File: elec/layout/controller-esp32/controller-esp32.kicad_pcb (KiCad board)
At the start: 2 copper layers, 41 parts, among them U1 10nF ±10% 50V X7R, U10 12.4kΩ ±1% 62.5mW, U11 1nF ±10% 50V X7R, U12 220Ω ±1% 62.5mW, U13 1MΩ ±1% 62.5mW, U15 10pF ±5% 50V C0G, U16 10pF ±5% 50V C0G, U17 100Ω ±1% 62.5mW, U19 10nF ±10% 50V X7R, U2 220Ω ±1% 62.5mW, U20 6.8nF ±10% 50V X7R, U21 33Ω ±1% 62.5mW, U22 49.9Ω ±1% 62.5mW, U23 6.8nF ±10% 50V X7R, U24 33Ω ±1% 62.5mW, U25 49.9Ω ±1% 62.5mW, U26 4.7µF ±10% 10V X5R, U27 22nF ±10% 50V X7R, U28 10Ω ±1% 62.5mW, U29 33Ω ±1% 62.5mW, U3 10µF ±10% 25V X5R, U30 49.9Ω ±1% 62.5mW, U31 33Ω ±1% 62.5mW, U32 49.9Ω ±1% 62.5mW, U34 10µF ±10% 25V X5R, U35 10µF ±10% 25V X5R, U37 10kΩ ±1% 62.5mW, U39 100nF ±10% 16V X7R, U4 100nF ±10% 16V X7R, U41 10kΩ ±1% 62.5mW, U5 100nF ±10% 16V X7R, U6 100nF ±10% 16V X7R, U7 100nF ±10% 16V X7R, U8 100nF ±10% 16V X7R, U9 100nF ±10% 16V X7R

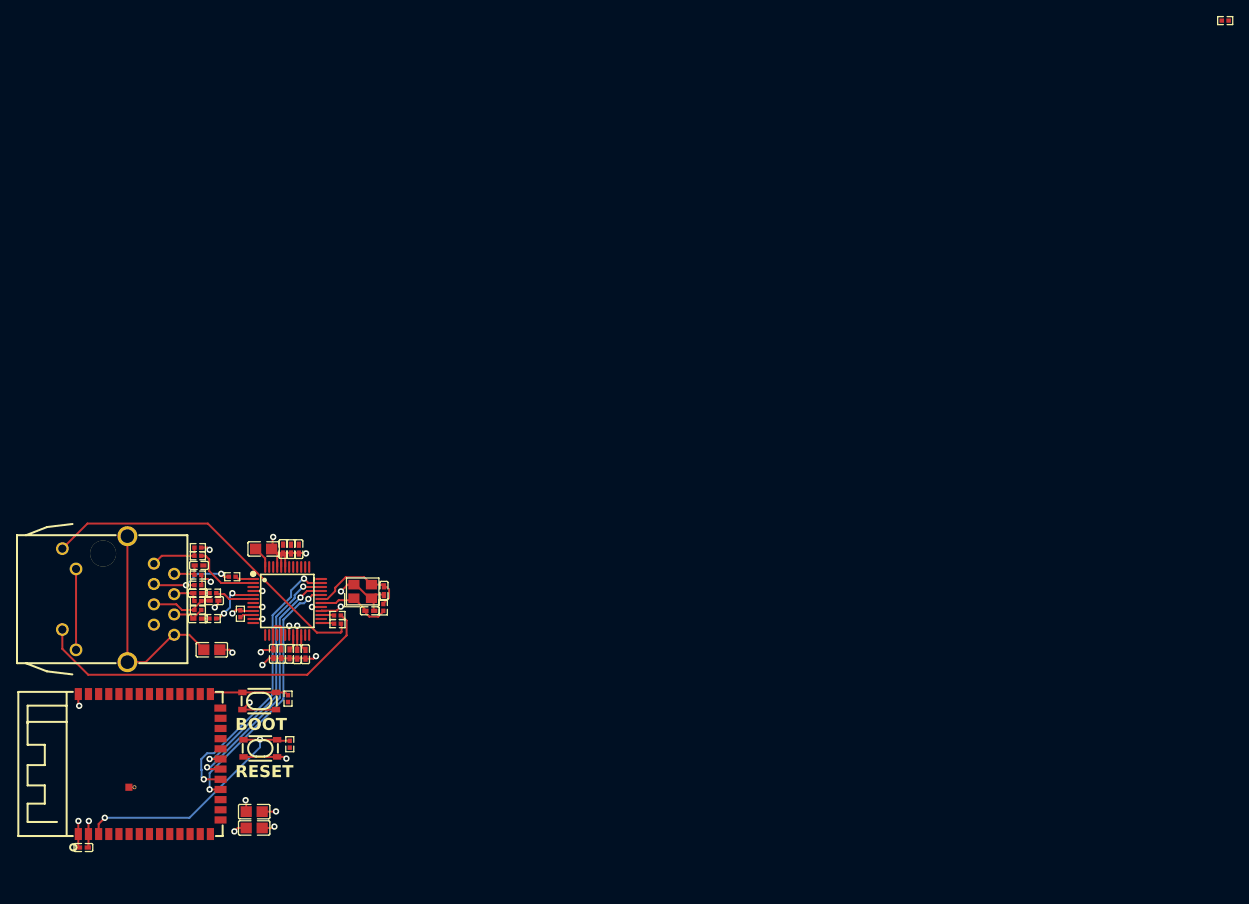
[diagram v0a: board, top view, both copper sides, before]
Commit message: remove default build, build everything locally
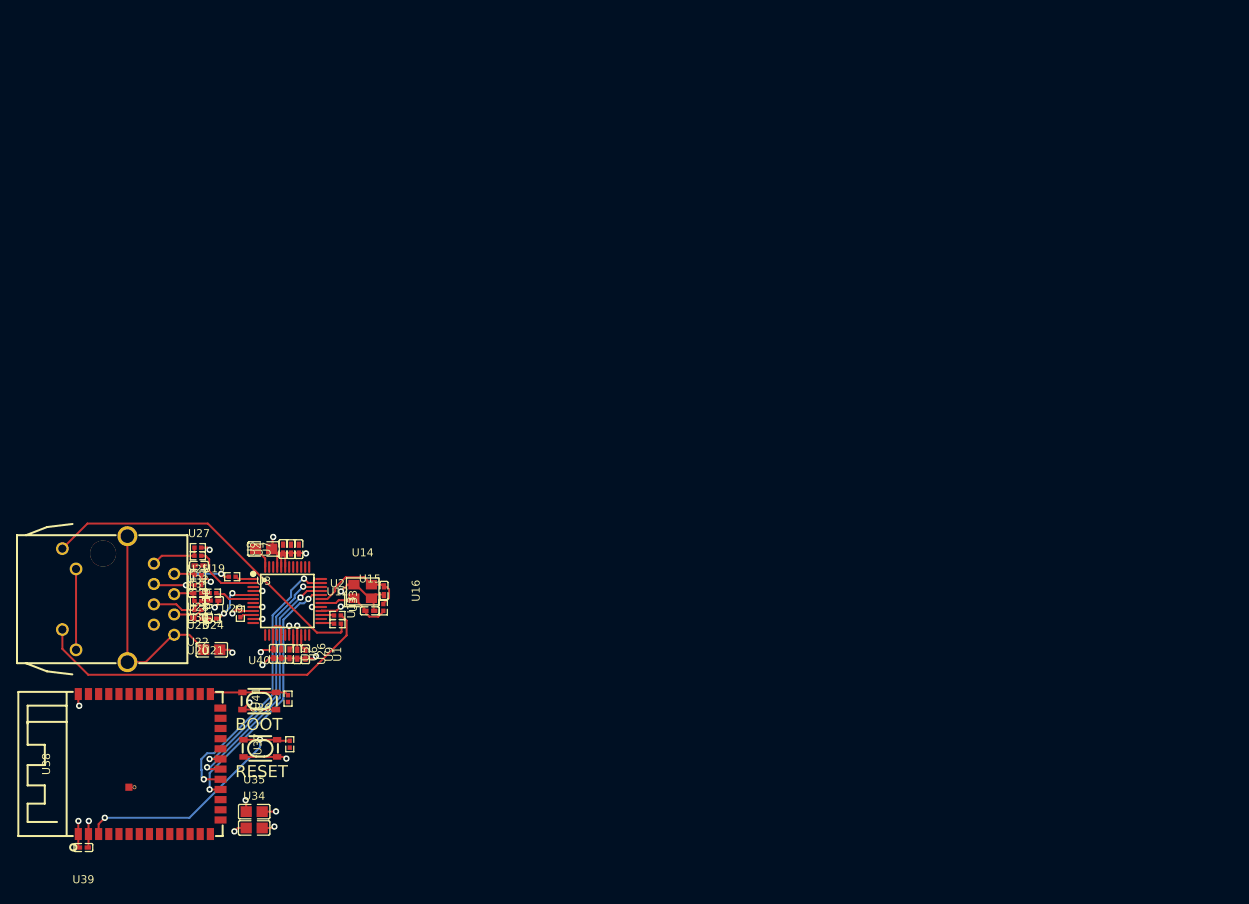
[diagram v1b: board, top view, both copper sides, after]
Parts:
- removed U17: 100Ω ±1% 62.5mW, atopile:R0402-56259e
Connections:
- U36 pad 1: in -> in-1
- U36 pad 2: in -> in-1
- U37 pad 2: in -> in-1
- U38 pad 27: in-1 -> in
- U38 pad 3: in -> in-1
- U40 pad 1: in-1 -> in
- U40 pad 2: in-1 -> in
- U41 pad 2: in-1 -> in
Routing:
- net in-1: track 9.92 -> 32.2 mm, vias 0 -> 2
- net in: track 32.2 -> 9.92 mm, vias 2 -> 0

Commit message: add module builds back in to ato.yaml with mfg-data excluded in config
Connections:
- U20 pad 1: ethernet-net -> ethernet-net-1
- U21 pad 2: ethernet-net -> ethernet-net-1
- U23 pad 1: ethernet-net-1 -> ethernet-net
- U24 pad 2: ethernet-net-1 -> ethernet-net
- U38 pad 6: line-1 -> line
- U38 pad 7: line -> line-1
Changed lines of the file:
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@@
             (outputdirectory "")))
     (net 0 "")
-    (net 1 "line")
+    (net 1 "line-1")
     (net 2 "RD_minus")
     (net 3 "io14")
@@
     (net 23 "tck")
     (net 24 "ACTLED")
-    (net 25 "ethernet-net-1")
+    (net 25 "ethernet-net")
     (net 26 "SPDLED")
     (net 27 "io37")
@@
     (net 30 "dm")
     (net 31 "io45")
-    (net 32 "ethernet-net")
+    (net 32 "ethernet-net-1")
     (net 33 "miso")
     (net 34 "VBG")
@@
     (net 64 "gnd")
     (net 65 "io2")
-    (net 66 "line-1")
+    (net 66 "line")
     (net 67 "LINKLED")
     (net 68 "in")
@@
             (layers "F.Cu" "F.Paste" "F.Mask")
             (remove_unused_layers no)
-            (net 25 "ethernet-net-1"))
+            (net 25 "ethernet-net"))
         (pad "2" smd rect
             (at 0.55 0 180)
@@
             (layers "F.Cu" "F.Paste" "F.Mask")
             (remove_unused_layers no)
-            (net 66 "line-1"))
+            (net 66 "line"))
         (pad "7" smd rect
             (at -8.75 -1.27 90)
@@
             (layers "F.Cu" "F.Paste" "F.Mask")
             (remove_unused_layers no)
-            (net 1 "line"))
+            (net 1 "line-1"))
         (pad "8" smd rect
             (at -8.75 0 90)
@@
             (layers "F.Cu" "F.Paste" "F.Mask")
             (remove_unused_layers no)
-            (net 32 "ethernet-net"))
+            (net 32 "ethernet-net-1"))
         (pad "2" smd rect
             (at 0.55 0 180)
@@
             (layers "F.Cu" "F.Paste" "F.Mask")
             (remove_unused_layers no)
-            (net 32 "ethernet-net")))
+            (net 32 "ethernet-net-1")))
     (footprint "atopile:C0402-b3ef17"
         (layer "F.Cu")
@@
             (layers "F.Cu" "F.Paste" "F.Mask")
             (remove_unused_layers no)
-            (net 25 "ethernet-net-1")))
+            (net 25 "ethernet-net")))
     (footprint "atopile:C0402-b3ef17"
         (layer "F.Cu")

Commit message: add CAN communication block and RPI CM4 block
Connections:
- U36 pad 1: in-1 -> in
- U36 pad 2: in-1 -> in
- U37 pad 2: in-1 -> in
- U38 pad 27: in -> in-1
- U38 pad 3: in-1 -> in
- U40 pad 1: in -> in-1
- U40 pad 2: in -> in-1
- U41 pad 2: in -> in-1
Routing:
- net in-1: track 32.2 -> 9.92 mm, vias 2 -> 0
- net in: track 9.92 -> 32.2 mm, vias 0 -> 2

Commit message: add CAN isolator, cellsim cell
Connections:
- U20 pad 1: ethernet-net-1 -> ethernet-net
- U21 pad 2: ethernet-net-1 -> ethernet-net
- U23 pad 1: ethernet-net -> ethernet-net-1
- U24 pad 2: ethernet-net -> ethernet-net-1
- U36 pad 1: in -> in-1
- U36 pad 2: in -> in-1
- U37 pad 2: in -> in-1
- U38 pad 27: in-1 -> in
- U38 pad 3: in -> in-1
- U40 pad 1: in-1 -> in
- U40 pad 2: in-1 -> in
- U41 pad 2: in-1 -> in
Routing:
- net in-1: track 9.92 -> 32.2 mm, vias 0 -> 2
- net in: track 32.2 -> 9.92 mm, vias 2 -> 0
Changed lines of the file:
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@@
     (net 23 "tck")
     (net 24 "ACTLED")
-    (net 25 "ethernet-net")
+    (net 25 "ethernet-net-1")
     (net 26 "SPDLED")
     (net 27 "io37")
@@
     (net 30 "dm")
     (net 31 "io45")
-    (net 32 "ethernet-net-1")
+    (net 32 "ethernet-net")
     (net 33 "miso")
     (net 34 "VBG")
@@
     (net 53 "io48")
     (net 54 "RXD0")
-    (net 55 "in")
+    (net 55 "in-1")
     (net 56 "TD_plus")
     (net 57 "io38")
@@
     (net 64 "line")
     (net 65 "LINKLED")
-    (net 66 "in-1")
+    (net 66 "in")
     (footprint "atopile:R0402-56259e"
         (layer "F.Cu")
@@
             (layers "F.Cu" "F.Paste" "F.Mask")
             (remove_unused_layers no)
-            (net 25 "ethernet-net"))
+            (net 25 "ethernet-net-1"))
         (pad "2" smd rect
             (at 0.55 0 180)
@@
             (layers "F.Cu" "F.Paste" "F.Mask")
             (remove_unused_layers no)
-            (net 55 "in"))
+            (net 55 "in-1"))
         (pad "4" smd rect
             (at -8.75 -5.08 90)
@@
             (layers "F.Cu" "F.Paste" "F.Mask")
             (remove_unused_layers no)
-            (net 66 "in-1"))
+            (net 66 "in"))
         (pad "28" smd rect
             (at 8.75 6.35 270)
@@
             (layers "F.Cu" "F.Paste" "F.Mask")
             (remove_unused_layers no)
-            (net 66 "in-1")))
+            (net 66 "in")))
     (footprint "atopile:C0402-b3ef17"
         (layer "F.Cu")
@@
             (layers "F.Cu" "F.Paste" "F.Mask")
             (remove_unused_layers no)
-            (net 32 "ethernet-net-1"))
+            (net 32 "ethernet-net"))
         (pad "2" smd rect
             (at 0.55 0 180)
@@
             (layers "F.Cu" "F.Paste" "F.Mask")
             (remove_unused_layers no)
-            (net 32 "ethernet-net-1")))
+            (net 32 "ethernet-net")))
     (footprint "atopile:C0402-b3ef17"
         (layer "F.Cu")
@@
             (layers "F.Cu" "F.Paste" "F.Mask")
             (remove_unused_layers no)
-            (net 66 "in-1"))
+            (net 66 "in"))
         (pad "2" smd rect
             (at 2.1 -1.07 0)
@@
             (layers "F.Cu" "F.Paste" "F.Mask")
             (remove_unused_layers no)
-            (net 66 "in-1"))
+            (net 66 "in"))
         (pad "3" smd rect
             (at -2.1 1.07 0)
@@
             (layers "F.Cu" "F.Paste" "F.Mask")
             (remove_unused_layers no)
-            (net 55 "in"))
+            (net 55 "in-1"))
         (pad "2" smd rect
             (at 2.1 -1.07 0)
@@
             (layers "F.Cu" "F.Paste" "F.Mask")
             (remove_unused_layers no)
-            (net 55 "in"))
+            (net 55 "in-1"))
         (pad "3" smd rect
             (at -2.1 1.07 0)
@@
             (layers "F.Cu" "F.Paste" "F.Mask")
             (remove_unused_layers no)
-            (net 25 "ethernet-net")))
+            (net 25 "ethernet-net-1")))
     (footprint "atopile:C0402-b3ef17"
         (layer "F.Cu")
@@
             (layers "F.Cu" "F.Paste" "F.Mask")
             (remove_unused_layers no)
-            (net 55 "in")))
+            (net 55 "in-1")))
     (via
         (at 142.575 106.69)

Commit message: rebuild all modules
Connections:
- U20 pad 1: ethernet-net -> ethernet-net-1
- U21 pad 2: ethernet-net -> ethernet-net-1
- U23 pad 1: ethernet-net-1 -> ethernet-net
- U24 pad 2: ethernet-net-1 -> ethernet-net
- U36 pad 1: in-1 -> in
- U36 pad 2: in-1 -> in
- U37 pad 2: in-1 -> in
- U38 pad 27: in -> in-1
- U38 pad 3: in-1 -> in
- U40 pad 1: in -> in-1
- U40 pad 2: in -> in-1
- U41 pad 2: in -> in-1
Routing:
- net in-1: track 32.2 -> 9.92 mm, vias 2 -> 0
- net in: track 9.92 -> 32.2 mm, vias 0 -> 2
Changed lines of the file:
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@@
     (net 23 "tck")
     (net 24 "ACTLED")
-    (net 25 "ethernet-net-1")
+    (net 25 "ethernet-net")
     (net 26 "SPDLED")
     (net 27 "io37")
@@
     (net 30 "dm")
     (net 31 "io45")
-    (net 32 "ethernet-net")
+    (net 32 "ethernet-net-1")
     (net 33 "miso")
     (net 34 "VBG")
@@
     (net 53 "io48")
     (net 54 "RXD0")
-    (net 55 "in-1")
+    (net 55 "in")
     (net 56 "TD_plus")
     (net 57 "io38")
@@
     (net 64 "line")
     (net 65 "LINKLED")
-    (net 66 "in")
+    (net 66 "in-1")
     (footprint "atopile:R0402-56259e"
         (layer "F.Cu")
@@
             (layers "F.Cu" "F.Paste" "F.Mask")
             (remove_unused_layers no)
-            (net 25 "ethernet-net-1"))
+            (net 25 "ethernet-net"))
         (pad "2" smd rect
             (at 0.55 0 180)
@@
             (layers "F.Cu" "F.Paste" "F.Mask")
             (remove_unused_layers no)
-            (net 55 "in-1"))
+            (net 55 "in"))
         (pad "4" smd rect
             (at -8.75 -5.08 90)
@@
             (layers "F.Cu" "F.Paste" "F.Mask")
             (remove_unused_layers no)
-            (net 66 "in"))
+            (net 66 "in-1"))
         (pad "28" smd rect
             (at 8.75 6.35 270)
@@
             (layers "F.Cu" "F.Paste" "F.Mask")
             (remove_unused_layers no)
-            (net 66 "in")))
+            (net 66 "in-1")))
     (footprint "atopile:C0402-b3ef17"
         (layer "F.Cu")
@@
             (layers "F.Cu" "F.Paste" "F.Mask")
             (remove_unused_layers no)
-            (net 32 "ethernet-net"))
+            (net 32 "ethernet-net-1"))
         (pad "2" smd rect
             (at 0.55 0 180)
@@
             (layers "F.Cu" "F.Paste" "F.Mask")
             (remove_unused_layers no)
-            (net 32 "ethernet-net")))
+            (net 32 "ethernet-net-1")))
     (footprint "atopile:C0402-b3ef17"
         (layer "F.Cu")
@@
             (layers "F.Cu" "F.Paste" "F.Mask")
             (remove_unused_layers no)
-            (net 66 "in"))
+            (net 66 "in-1"))
         (pad "2" smd rect
             (at 2.1 -1.07 0)
@@
             (layers "F.Cu" "F.Paste" "F.Mask")
             (remove_unused_layers no)
-            (net 66 "in"))
+            (net 66 "in-1"))
         (pad "3" smd rect
             (at -2.1 1.07 0)
@@
             (layers "F.Cu" "F.Paste" "F.Mask")
             (remove_unused_layers no)
-            (net 55 "in-1"))
+            (net 55 "in"))
         (pad "2" smd rect
             (at 2.1 -1.07 0)
@@
             (layers "F.Cu" "F.Paste" "F.Mask")
             (remove_unused_layers no)
-            (net 55 "in-1"))
+            (net 55 "in"))
         (pad "3" smd rect
             (at -2.1 1.07 0)
@@
             (layers "F.Cu" "F.Paste" "F.Mask")
             (remove_unused_layers no)
-            (net 25 "ethernet-net-1")))
+            (net 25 "ethernet-net")))
     (footprint "atopile:C0402-b3ef17"
         (layer "F.Cu")
@@
             (layers "F.Cu" "F.Paste" "F.Mask")
             (remove_unused_layers no)
-            (net 55 "in-1")))
+            (net 55 "in")))
     (via
         (at 142.575 106.69)

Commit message: core layout, rebuild modules with compiler updates
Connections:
- U20 pad 1: ethernet-net-1 -> ethernet-net
- U21 pad 2: ethernet-net-1 -> ethernet-net
- U23 pad 1: ethernet-net -> ethernet-net-1
- U24 pad 2: ethernet-net -> ethernet-net-1
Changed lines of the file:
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@@
     (net 23 "tck")
     (net 24 "ACTLED")
-    (net 25 "ethernet-net")
+    (net 25 "ethernet-net-1")
     (net 26 "SPDLED")
     (net 27 "io37")
@@
     (net 30 "dm")
     (net 31 "io45")
-    (net 32 "ethernet-net-1")
+    (net 32 "ethernet-net")
     (net 33 "miso")
     (net 34 "VBG")
@@
             (layers "F.Cu" "F.Paste" "F.Mask")
             (remove_unused_layers no)
-            (net 25 "ethernet-net"))
+            (net 25 "ethernet-net-1"))
         (pad "2" smd rect
             (at 0.55 0 180)
@@
             (layers "F.Cu" "F.Paste" "F.Mask")
             (remove_unused_layers no)
-            (net 32 "ethernet-net-1"))
+            (net 32 "ethernet-net"))
         (pad "2" smd rect
             (at 0.55 0 180)
@@
             (layers "F.Cu" "F.Paste" "F.Mask")
             (remove_unused_layers no)
-            (net 32 "ethernet-net-1")))
+            (net 32 "ethernet-net")))
     (footprint "atopile:C0402-b3ef17"
         (layer "F.Cu")
@@
             (layers "F.Cu" "F.Paste" "F.Mask")
             (remove_unused_layers no)
-            (net 25 "ethernet-net")))
+            (net 25 "ethernet-net-1")))
     (footprint "atopile:C0402-b3ef17"
         (layer "F.Cu")
